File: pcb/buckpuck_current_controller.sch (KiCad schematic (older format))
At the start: 17 parts, among them P1 POWER, P2 ResetOverride, P3 Display, P4 Switches, P5 CONN_1, P6 CONN_1, P7 CONN_1, P8 CONN_1, U1 V7809, U2 ARDUINO_NANO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

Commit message: Completed board design version 2.
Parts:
- removed U3: MCP434X/436X, symbol MCP434X/436X
- added C6: 0.1uF, symbol C
- added U3, U4: MCP42X1-PDIP, symbol MCP42X1-PDIP
- added U5: NOT_GATE, symbol NOT_GATE
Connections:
- net labels added: CSNot
- wire segments 126 -> 146
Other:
- moved on the sheet: C5, P4, P5, P6, P7, P8

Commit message: Initial changes for version-3 design
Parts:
- removed C5, C6: 0.1uF, symbol C
- removed U3, U4: MCP42X1-PDIP, symbol MCP42X1-PDIP
- removed U5: NOT_GATE, symbol NOT_GATE
- added D?: AD57X4R, symbol AD57X4R
- added P?: CONN_4X2, symbol CONN_4X2
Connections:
- net labels added: A2, A3, A4, A5, ControlA, ControlB, ControlC, ControlD, D2, D3, D4
- net labels removed: CSNot, CurrentSenseA, CurrentSenseB, CurrentSenseC, CurrentSenseD, P0A, P0B, P0W, P1A, P1B, P1W, P2A, P2B, P2W, P3A, P3B, P3W, SwitchE, SwitchF
- wire segments 146 -> 125
- no-connect marks 7 -> 11

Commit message: Finished schematic version 3
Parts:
- removed C1, C2, C3: 10uF, symbol C
- added B1: BUFFER_EL5227, symbol BUFFER_EL5227
- added C1, C10, C2, C3, C6: 10uF, symbol CAPAPOL
- added C11, C5, C7, C9: 0.1uF, symbol C
- added C8: 4.7uF, symbol CAPAPOL
- P13: renamed from P?; value CONN_4X2 -> I/O
- P4: value Switches -> I/O
- gave numbers to parts that had none: 1
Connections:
- net labels added: VoutA, VoutB, VoutC, VoutD
- net labels removed: D4
- wire segments 125 -> 158
- no-connect marks 11 -> 15
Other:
- moved on the sheet: D1, P3

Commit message: Made changes to schematic, board, and bom
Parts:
- removed C1, C2, C3: 10uF, symbol CAPAPOL
- added C1, C2, C3: 10uF, symbol C
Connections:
- net GND: now also C1.2, C2.2, C3.2
- net VAA: now also C1.1, C2.1
- net VDD: now also C3.1
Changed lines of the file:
@@
-EESchema Schematic File Version 2  date Tue 12 Jul 2011 03:30:38 PM PDT
+EESchema Schematic File Version 2  date Wed 13 Jul 2011 06:58:13 PM PDT
 LIBS:power
 LIBS:device
@@
 Sheet 1 5
 Title "Buckpuck Current Controller"
-Date "12 jul 2011"
+Date "14 jul 2011"
 Rev "3.0"
 Comp ""
@@
 Comment4 ""
 $EndDescr
+Text Label 2450 2900 0    60   ~ 0
+PowerIn-
+Text Label 2500 1800 0    60   ~ 0
+PowerIn+
+Wire Wire Line
+	5750 2300 5750 2450
+Wire Wire Line
+	4250 1900 4250 1800
+Wire Wire Line
+	3450 2300 3450 2900
 Connection ~ 3200 2900
 Wire Wire Line
-	3450 2300 3450 2900
-Wire Wire Line
 	3450 2900 2350 2900
-Wire Wire Line
-	4250 2300 4250 2450
-Wire Wire Line
-	5750 2300 5750 2450
 Connection ~ 4250 5700
 Wire Wire Line
@@
 	3700 6600 3450 6600
 Wire Wire Line
-	4450 6150 4050 6150
-Wire Wire Line
-	4450 5750 4050 5750
+	4050 6150 4450 6150
+Wire Wire Line
+	4050 5750 4450 5750
 Wire Wire Line
 	4250 6300 4250 6150
@@
 	3950 7250 3950 7400
 Wire Wire Line
-	4150 6850 3750 6850
-Wire Wire Line
-	3450 6700 3950 6700
+	3750 6850 4150 6850
+Wire Wire Line
+	3950 6700 3450 6700
 Wire Wire Line
 	2450 6150 2450 6100
@@
 Connection ~ 5650 6100
 Wire Wire Line
-	5650 6100 6250 6100
+	6250 6100 5650 6100
 Connection ~ 7250 6200
 Wire Wire Line
@@
 Connection ~ 3450 1800
 Wire Wire Line
-	2950 2900 2950 2750
+	2950 2750 2950 2900
 Wire Wire Line
 	3200 2900 3200 3050
@@
 Connection ~ 6050 6500
 Wire Wire Line
-	7250 6700 7250 6100
+	7250 6100 7250 6700
 Wire Wire Line
 	5650 6200 6250 6200
@@
 Connection ~ 7250 6100
 Wire Wire Line
-	5650 5750 5650 6300
+	5650 6300 5650 5750
 Connection ~ 5650 6200
 Wire Wire Line
@@
 Connection ~ 3550 6700
 Wire Wire Line
-	4150 7250 3750 7250
+	3750 7250 4150 7250
 Wire Wire Line
 	3950 6600 3950 6850
@@
 	4250 5550 4250 5750
 Connection ~ 4250 5750
+Connection ~ 5750 1800
+Connection ~ 4250 1800
+Wire Wire Line
+	3450 1900 3450 1500
+Wire Wire Line
+	4250 2300 4250 2450
 Wire Wire Line
 	5750 1900 5750 1800
-Connection ~ 5750 1800
-Wire Wire Line
-	4250 1800 4250 1900
-Connection ~ 4250 1800
-Wire Wire Line
-	3450 1900 3450 1500
 $Comp
-L CAPAPOL C1
-U 1 1 4E1CA1AE
-P 3450 2100
-F 0 "C1" H 3500 2200 50  0000 L CNN
-F 1 "10uF" H 3500 2000 50  0000 L CNN
-	1    3450 2100
+L C C3
+U 1 1 4E1E4A21
+P 5750 2100
+F 0 "C3" H 5800 2200 50  0000 L CNN
+F 1 "10uF" H 5800 2000 50  0000 L CNN
+	1    5750 2100
 	1    0    0    -1
 $EndComp
 $Comp
-L CAPAPOL C2
-U 1 1 4E1CA18D
+L C C2
+U 1 1 4E1E49E0
 P 4250 2100
 F 0 "C2" H 4300 2200 50  0000 L CNN
@@
 $EndComp
 $Comp
-L CAPAPOL C3
-U 1 1 4E1CA16A
-P 5750 2100
-F 0 "C3" H 5800 2200 50  0000 L CNN
-F 1 "10uF" H 5800 2000 50  0000 L CNN
-	1    5750 2100
+L C C1
+U 1 1 4E1E49B6
+P 3450 2100
+F 0 "C1" H 3500 2200 50  0000 L CNN
+F 1 "10uF" H 3500 2000 50  0000 L CNN
+	1    3450 2100
 	1    0    0    -1
 $EndComp

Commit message: Finished version 3
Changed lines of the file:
@@
-EESchema Schematic File Version 2  date Wed 13 Jul 2011 06:58:13 PM PDT
+EESchema Schematic File Version 2  date Thu 14 Jul 2011 12:12:51 PM PDT
 LIBS:power
 LIBS:device
@@
 Comment4 ""
 $EndDescr
-Text Label 2450 2900 0    60   ~ 0
-PowerIn-
-Text Label 2500 1800 0    60   ~ 0
-PowerIn+
 Wire Wire Line
 	5750 2300 5750 2450

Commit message: Made intial version-4 changes to the schematic
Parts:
- P13: value I/O -> BNC
- P4: value I/O -> Switches
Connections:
- net PotentiometerC is gone; now on net BNC_C: U2.25 (A6)
- net PotentiometerD is gone; now on net BNC_D: U2.26 (A7)
- net ControlA: no longer B1.20 (Vout1)
- net ControlB: no longer B1.19 (Vout2)
- net D2: no longer P4.11
- net D3: no longer P4.9
- net PotentiometerA: no longer U2.19 (A0(PC0)(ADC0))
- net PotentiometerB: no longer U2.20 (A1(PC1)(ADC1))
- net SwitchA: no longer P4.1 (P1)
- net SwitchB: no longer P4.3 (P3)
- net SwitchC: no longer P4.5 (P5)
- net SwitchD: no longer P4.7 (P7)
- net A2 renamed BNC_A
- net BNC_A: now also U2.23 (A4(PC4)(SDA)); no longer U2.21 (A2(PC2)(ADC2))
- net A3 renamed BNC_B
- net BNC_B: now also U2.24 (A5(PC5)(SCL)); no longer U2.22 (A3(PC3)(ADC3))
- net A4 renamed BNC_C
- net BNC_C: no longer U2.23 (A4(PC4)(SDA))
- net A5 renamed BNC_D
- net BNC_D: no longer U2.24 (A5(PC5)(SCL))
- net CS renamed CS_DAC
- net ControlC renamed Buckpuck_Control_C
- net ControlD renamed Buckpuck_Control_D
- net DisplayRX renamed Display_RX
- net DisplayTX renamed Display_TX
- net VoutA renamed Vout_A
- net VoutB renamed Vout_B
- net VoutC renamed Vout_C
- net VoutD renamed Vout_D
- new net Buckpuck_Control_A: B1.20 (Vout1)
- new net Buckpuck_Control_B: B1.19 (Vout2)
- new net Potentiometer_A: U2.19 (A0(PC0)(ADC0))
- new net Potentiometer_B: U2.20 (A1(PC1)(ADC1))
- new net Potentiometer_C: U2.21 (A2(PC2)(ADC2))
- new net Potentiometer_D: U2.22 (A3(PC3)(ADC3))
- new net Switch_A: P4.1 (P1)
- new net Switch_B: P4.3 (P3)
- new net Switch_C: P4.5 (P5)
- new net Switch_D: P4.7 (P7)
- new net Switch_Light: P4.11
- new net Switch_Set: P4.9
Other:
- moved on the sheet: B1, C1, C2, C3, C4, C5, C8, P1, P13, P2, P4, R1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

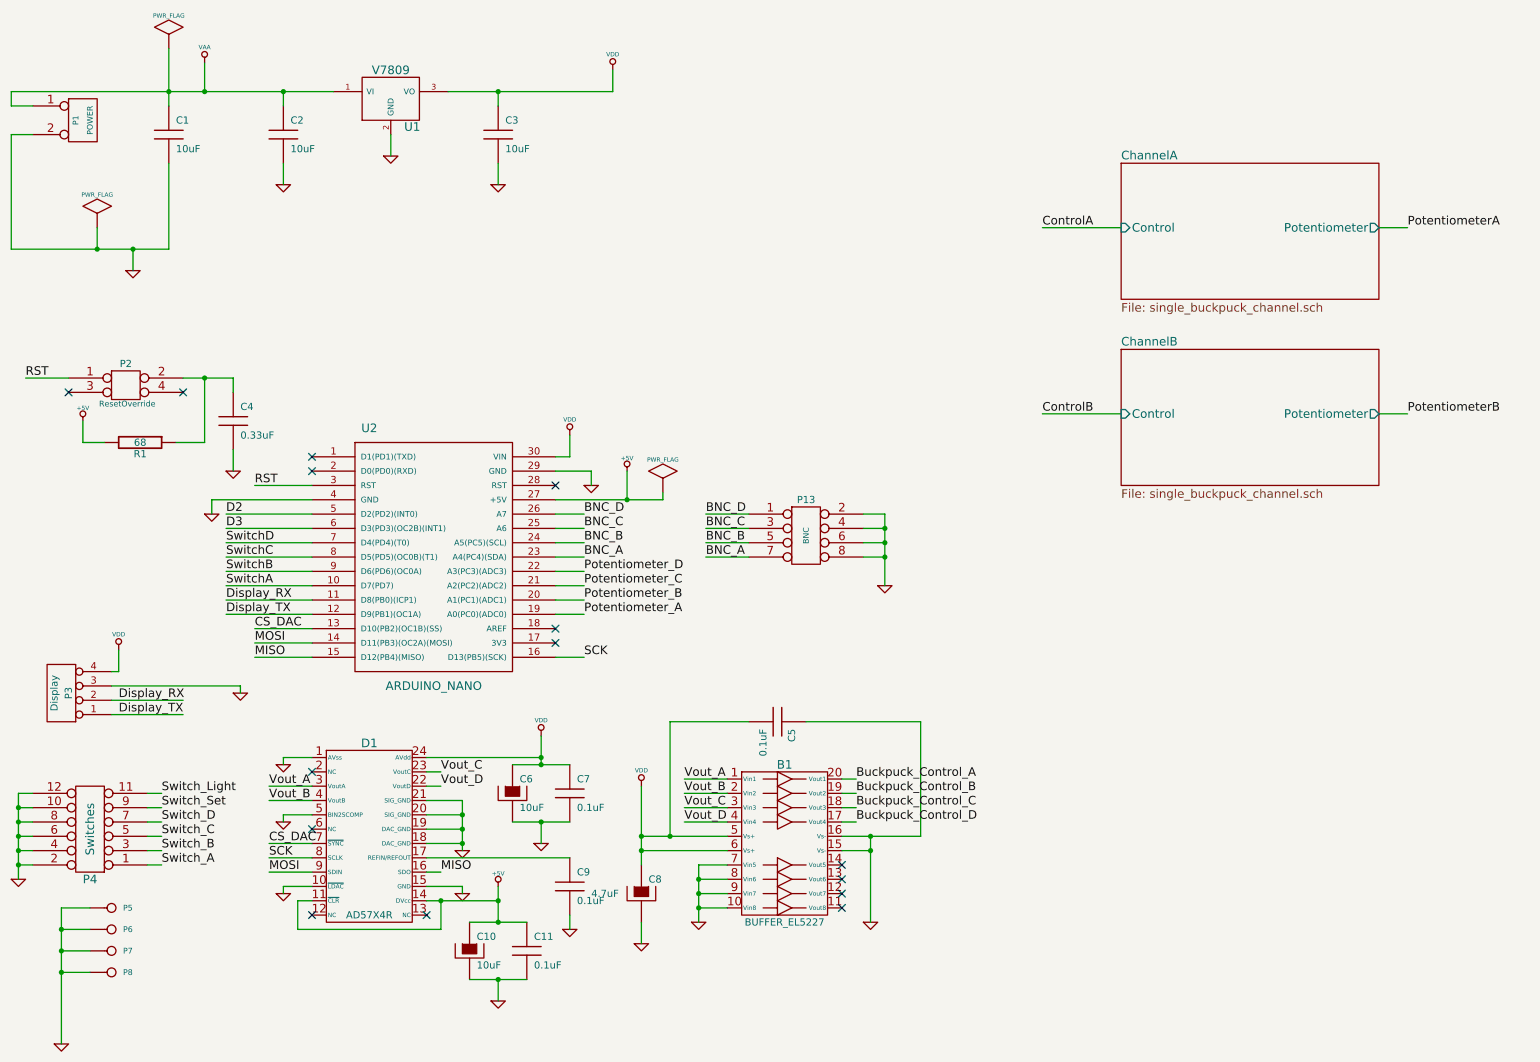
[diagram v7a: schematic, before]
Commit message: Added IO expander to the schematic
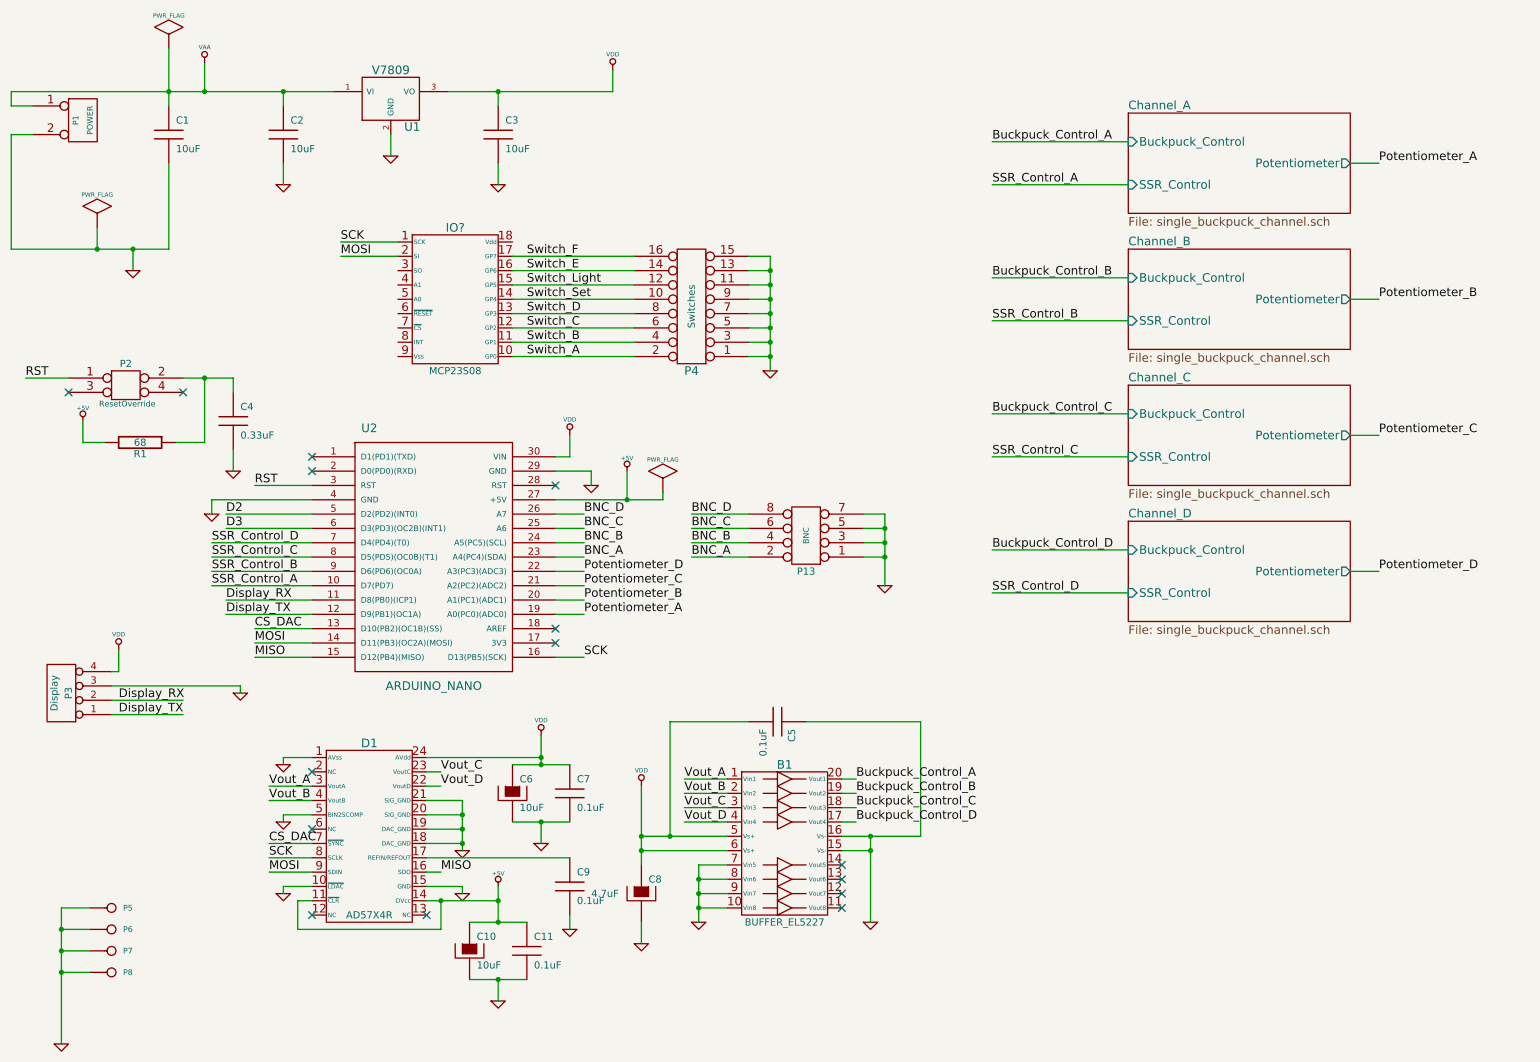
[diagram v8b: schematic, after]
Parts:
- removed P4: Switches, symbol CONN_6X2
- added IO?: MCP23S08, symbol MCP23S08
- added P4: Switches, symbol CONN_8X2
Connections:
- net BNC_A: now also P13.2; no longer P13.7
- net BNC_B: now also P13.4; no longer P13.5
- net BNC_C: now also P13.6; no longer P13.3
- net BNC_D: now also P13.8; no longer P13.1
- net GND: now also P13.1, P13.3, P13.5, P13.7, P4.1, P4.11, P4.13, P4.15, P4.3, P4.5, P4.7, P4.9; no longer P13.2, P13.4, P13.6, P13.8
- net MOSI: now also IO?.2 (SI)
- net SCK: now also IO?.1 (SCK)
- net Switch_A: now also IO?.10 (GP0), P4.2
- net Switch_B: now also IO?.11 (GP1), P4.4
- net Switch_C: now also IO?.12 (GP2), P4.6
- net Switch_D: now also IO?.13 (GP3), P4.8
- net Switch_Light: now also IO?.15 (GP5), P4.12
- net Switch_Set: now also IO?.14 (GP4), P4.10
- net SwitchA renamed SSR_Control_A
- net SwitchB renamed SSR_Control_B
- net SwitchC renamed SSR_Control_C
- net SwitchD renamed SSR_Control_D
- new net Switch_E: IO?.16 (GP6), P4.14
- new net Switch_F: IO?.17 (GP7), P4.16
